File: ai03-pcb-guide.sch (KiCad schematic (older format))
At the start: 14 parts

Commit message: Schematic complete
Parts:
- added D? (x4): SOD_123, symbol Device:D_Small
- added F?: 500mA, symbol Device:Polyfuse_Small
- added MX? (x4): MX-NoLED, symbol MX_Alps_Hybrid:MX-NoLED
- added USB?: Molex-0548190589, symbol random-keyboard-parts:Molex-0548190589
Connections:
- net +5V: now also F?.1
- net D+: now also USB?.3 (D+)
- net D-: now also USB?.4 (D-)
- net GND: now also USB?.1 (GND)
- new net: D?.2 (A), MX?.2 (ROW) (x4)
- new net COL0: MX?.1 (COL), MX?.1 (COL)
- new net COL1: MX?.1 (COL), MX?.1 (COL)
- new net ROW0: D?.1 (K), D?.1 (K)
- new net ROW1: D?.1 (K), D?.1 (K)
- new net VCC: F?.2, USB?.5 (VBUS)
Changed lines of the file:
@@
 Text GLabel 6750 2300 0    50   Input ~ 0
 D-
+$Comp
+L random-keyboard-parts:Molex-0548190589 USB?
+U 1 1 5F3CA75D
+P 4300 1600
+F 0 "USB?" V 4837 1567 60  0000 C CNN
+F 1 "Molex-0548190589" V 4731 1567 60  0000 C CNN
+F 2 "" H 4300 1600 60  0001 C CNN
+F 3 "" H 4300 1600 60  0001 C CNN
+	1    4300 1600
+	0    -1   -1   0
+$EndComp
+$Comp
+L power:VCC #PWR?
+U 1 1 5F3D50C6
+P 5250 1400
+F 0 "#PWR?" H 5250 1250 50  0001 C CNN
+F 1 "VCC" H 5267 1573 50  0000 C CNN
+F 2 "" H 5250 1400 50  0001 C CNN
+F 3 "" H 5250 1400 50  0001 C CNN
+	1    5250 1400
+	1    0    0    -1
+$EndComp
+$Comp
+L Device:Polyfuse_Small F?
+U 1 1 5F3D55C5
+P 5850 1400
+F 0 "F?" V 5645 1400 50  0000 C CNN
+F 1 "500mA" V 5736 1400 50  0000 C CNN
+F 2 "" H 5900 1200 50  0001 L CNN
+F 3 "~" H 5850 1400 50  0001 C CNN
+	1    5850 1400
+	0    1    1    0
+$EndComp
+$Comp
+L power:+5V #PWR?
+U 1 1 5F3D5B75
+P 6450 1400
+F 0 "#PWR?" H 6450 1250 50  0001 C CNN
+F 1 "+5V" H 6465 1573 50  0000 C CNN
+F 2 "" H 6450 1400 50  0001 C CNN
+F 3 "" H 6450 1400 50  0001 C CNN
+	1    6450 1400
+	1    0    0    -1
+$EndComp
+Wire Wire Line
+	4600 1400 5250 1400
+Wire Wire Line
+	5950 1400 6450 1400
+Connection ~ 5250 1400
+Wire Wire Line
+	5250 1400 5750 1400
+Text GLabel 4600 1500 2    50   Input ~ 0
+D-
+Text GLabel 4600 1600 2    50   Input ~ 0
+D+
+$Comp
+L power:GND #PWR?
+U 1 1 5F3D719E
+P 4750 1800
+F 0 "#PWR?" H 4750 1550 50  0001 C CNN
+F 1 "GND" H 4755 1627 50  0000 C CNN
+F 2 "" H 4750 1800 50  0001 C CNN
+F 3 "" H 4750 1800 50  0001 C CNN
+	1    4750 1800
+	1    0    0    -1
+$EndComp
+Wire Wire Line
+	4600 1800 4750 1800
+$Comp
+L MX_Alps_Hybrid:MX-NoLED MX?
+U 1 1 5F3DAE69
+P 4800 3300
+F 0 "MX?" H 4833 3523 60  0000 C CNN
+F 1 "MX-NoLED" H 4833 3449 20  0000 C CNN
+F 2 "" H 4175 3275 60  0001 C CNN
+F 3 "" H 4175 3275 60  0001 C CNN
+	1    4800 3300
+	1    0    0    -1
+$EndComp
+$Comp
+L Device:D_Small D?
+U 1 1 5F3DBACF
+P 4600 3550
+F 0 "D?" V 4646 3618 50  0000 L CNN
+F 1 "SOD_123" V 4555 3618 50  0000 L CNN
+F 2 "" V 4600 3550 50  0001 C CNN
+F 3 "~" V 4600 3550 50  0001 C CNN
+	1    4600 3550
+	0    1    -1   0
+$EndComp
+Wire Wire Line
+	4600 3450 4750 3450
+$Comp
+L MX_Alps_Hybrid:MX-NoLED MX?
+U 1 1 5F3E828C
+P 5300 3300
+F 0 "MX?" H 5333 3523 60  0000 C CNN
+F 1 "MX-NoLED" H 5333 3449 20  0000 C CNN
+F 2 "" H 4675 3275 60  0001 C CNN
+F 3 "" H 4675 3275 60  0001 C CNN
+	1    5300 3300
+	1    0    0    -1
+$EndComp
+$Comp
+L Device:D_Small D?
+U 1 1 5F3E8836
+P 5100 3550
+F 0 "D?" V 5146 3482 50  0000 R CNN
+F 1 "SOD_123" V 5055 3482 50  0000 R CNN
+F 2 "" V 5100 3550 50  0001 C CNN
+F 3 "~" V 5100 3550 50  0001 C CNN
+	1    5100 3550
+	0    -1   -1   0
+$EndComp
+Wire Wire Line
+	5100 3450 5250 3450
+$Comp
+L MX_Alps_Hybrid:MX-NoLED MX?
+U 1 1 5F3F6C96
+P 4800 3950
+F 0 "MX?" H 4833 4173 60  0000 C CNN
+F 1 "MX-NoLED" H 4833 4099 20  0000 C CNN
+F 2 "" H 4175 3925 60  0001 C CNN
+F 3 "" H 4175 3925 60  0001 C CNN
+	1    4800 3950
+	1    0    0    -1
+$EndComp
+$Comp
+L MX_Alps_Hybrid:MX-NoLED MX?
+U 1 1 5F3F71D4
+P 5300 3950
+F 0 "MX?" H 5333 4173 60  0000 C CNN
+F 1 "MX-NoLED" H 5333 4099 20  0000 C CNN
+F 2 "" H 4675 3925 60  0001 C CNN
+F 3 "" H 4675 3925 60  0001 C CNN
+	1    5300 3950
+	1    0    0    -1
+$EndComp
+$Comp
+L Device:D_Small D?
+U 1 1 5F3F9AF0
+P 4600 4200
+F 0 "D?" V 4646 4268 50  0000 L CNN
+F 1 "SOD_123" V 4555 4268 50  0000 L CNN
+F 2 "" V 4600 4200 50  0001 C CNN
+F 3 "~" V 4600 4200 50  0001 C CNN
+	1    4600 4200
+	0    1    -1   0
+$EndComp
+$Comp
+L Device:D_Small D?
+U 1 1 5F3F9EA1
+P 5100 4200
+F 0 "D?" V 5146 4268 50  0000 L CNN
+F 1 "SOD_123" V 5055 4268 50  0000 L CNN
+F 2 "" V 5100 4200 50  0001 C CNN
+F 3 "~" V 5100 4200 50  0001 C CNN
+	1    5100 4200
+	0    1    -1   0
+$EndComp
+Wire Wire Line
+	5100 4100 5250 4100
+Wire Wire Line
+	4600 4100 4750 4100
+Wire Wire Line
+	4950 3900 4950 3250
+Connection ~ 4950 3250
+Wire Wire Line
+	4950 3250 4950 3000
+Wire Wire Line
+	5450 3900 5450 3250
+Connection ~ 5450 3250
+Wire Wire Line
+	5450 3250 5450 3000
+Wire Wire Line
+	5100 3650 4600 3650
+Connection ~ 4600 3650
+Wire Wire Line
+	4600 3650 4300 3650
+Wire Wire Line
+	5100 4300 4600 4300
+Connection ~ 4600 4300
+Wire Wire Line
+	4600 4300 4300 4300
+Text GLabel 4950 3000 1    50   Input ~ 0
+COL0
+Text GLabel 5450 3000 1    50   Input ~ 0
+COL1
+Text GLabel 4300 3650 0    50   Input ~ 0
+ROW0
+Text GLabel 4300 4300 0    50   Input ~ 0
+ROW1
 $EndSCHEMATC

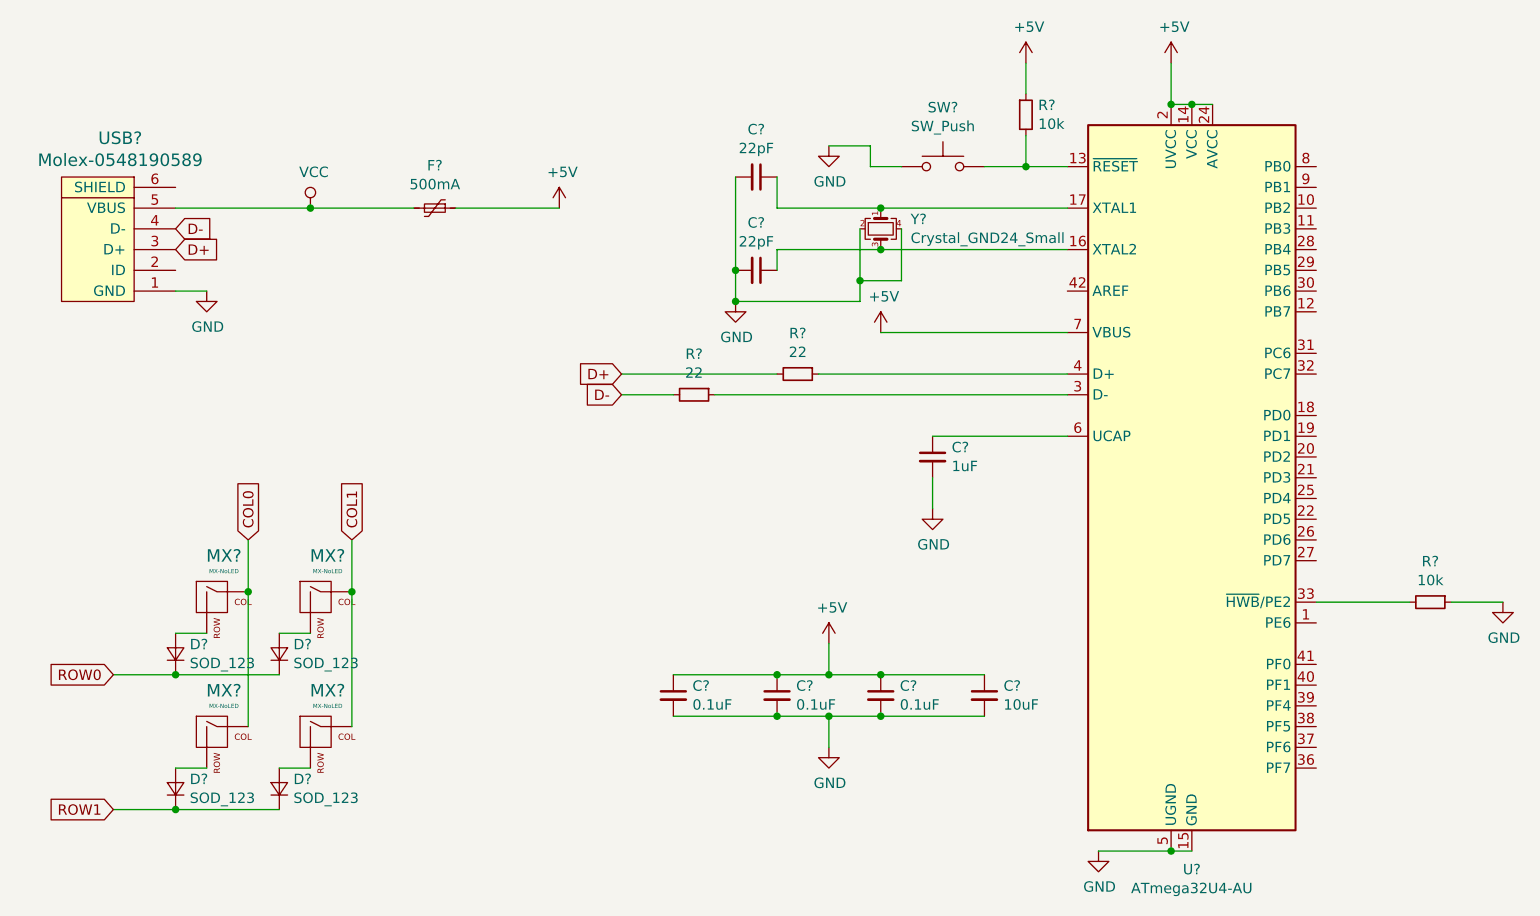
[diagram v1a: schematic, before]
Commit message: Applies footprints from schematic
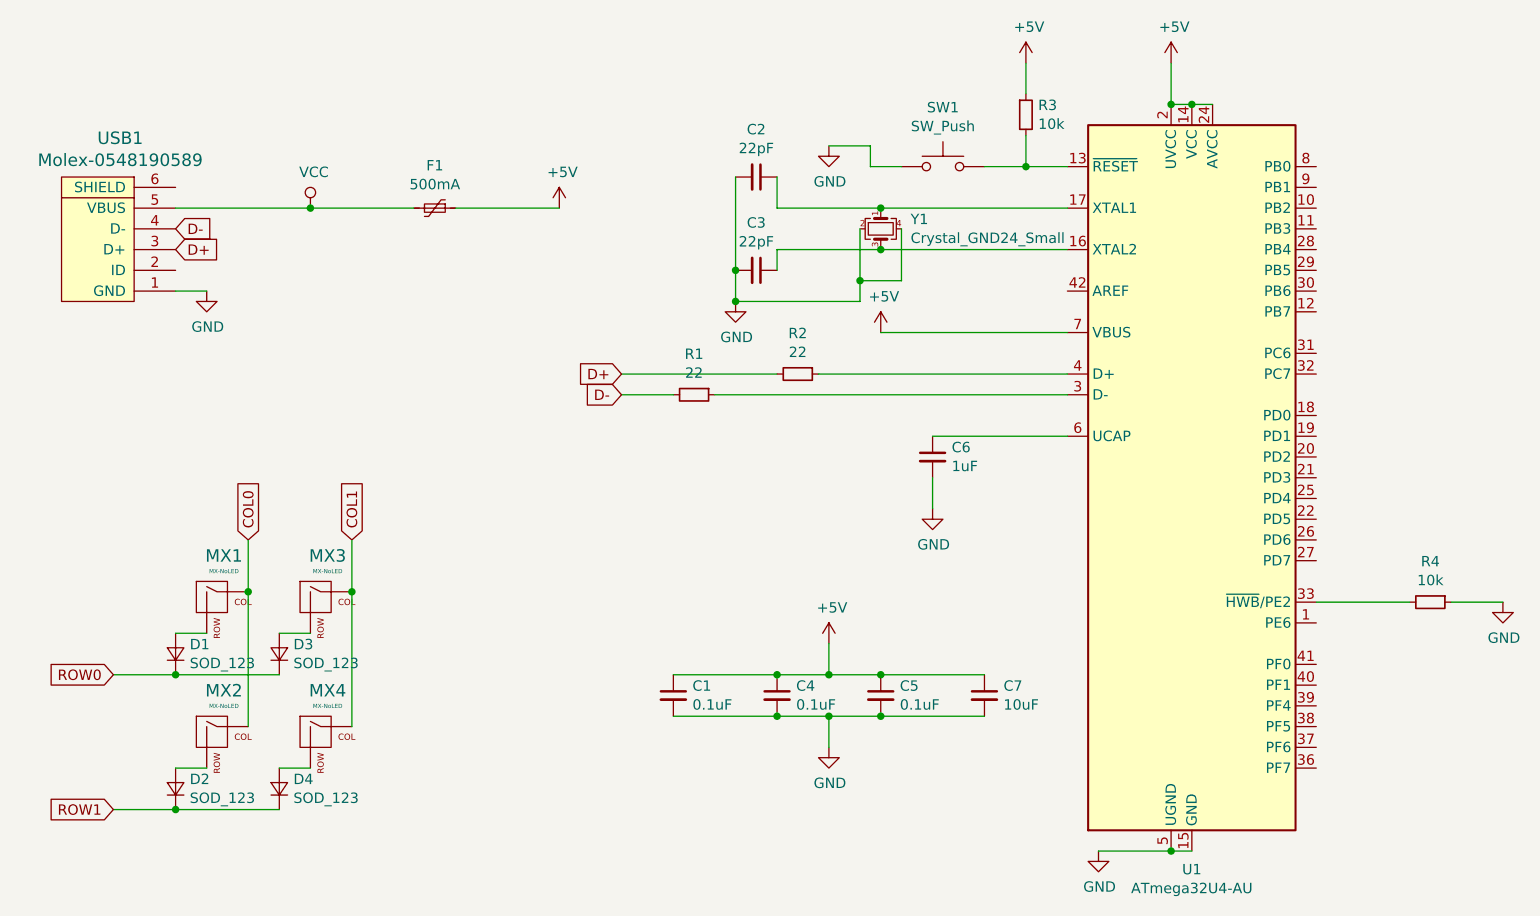
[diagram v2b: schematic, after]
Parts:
- C1, C2, C3, C4, C5, C6, C7: renamed from C?; footprint (none) -> Capacitor_SMD:C_0805_2012Metric
- D1, D2, D3, D4: renamed from D?; footprint (none) -> Diode_SMD:D_SOD-123
- F1: renamed from F?; footprint (none) -> Fuse:Fuse_1206_3216Metric
- MX1, MX2, MX3, MX4: renamed from MX?; footprint (none) -> MX_Alps_Hybrid:MX-1U-NoLED
- R1, R2, R3, R4: renamed from R?; footprint (none) -> Resistor_SMD:R_0805_2012Metric
- SW1: renamed from SW?; footprint (none) -> random-keyboard-parts:SKQG-1155865
- USB1: renamed from USB?; footprint (none) -> random-keyboard-parts:Molex-0548190589
- Y1: renamed from Y?; footprint (none) -> Crystal:Crystal_SMD_3225-4Pin_3.2x2.5mm
- gave numbers to parts that had none: 1

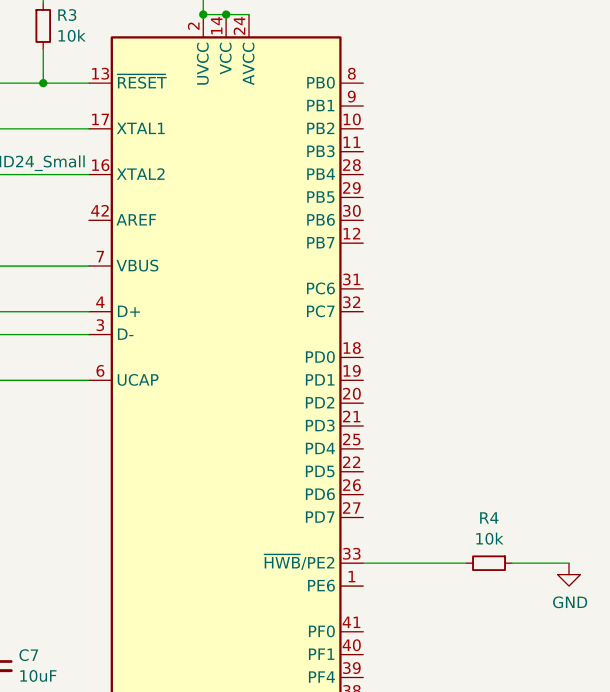
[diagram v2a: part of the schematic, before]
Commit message: Completes routing
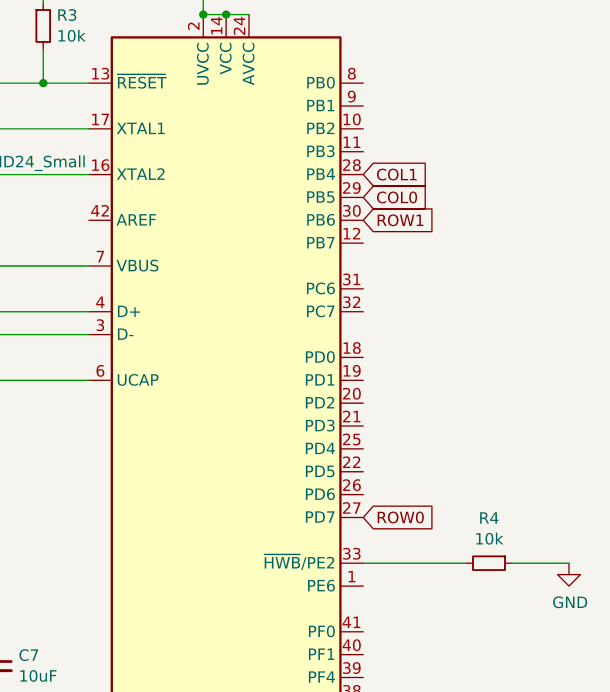
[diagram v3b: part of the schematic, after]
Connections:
- net COL0: now also U1.29 (PB5)
- net COL1: now also U1.28 (PB4)
- net ROW0: now also U1.27 (PD7)
- net ROW1: now also U1.30 (PB6)
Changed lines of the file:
@@
 Text GLabel 4300 4300 0    50   Input ~ 0
 ROW1
+Text GLabel 10100 3100 2    50   Input ~ 0
+ROW0
+Text GLabel 10100 1700 2    50   Input ~ 0
+COL0
+Text GLabel 10100 1600 2    50   Input ~ 0
+COL1
+Text GLabel 10100 1800 2    50   Input ~ 0
+ROW1
 $EndSCHEMATC
